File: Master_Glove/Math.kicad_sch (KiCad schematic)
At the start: 0 parts

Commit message: Circuit Log+Sub fait
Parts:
- added D2: 1N4148WS, Diode_SMD:D_SOD-323, symbol Diode:1N4148WS
- added R1: 4.7k, symbol Device:R
- added R2, R3: 2.2k, symbol Device:R
- added R4, R5: 37.4k, symbol Device:R
- added R6, R7: 10k, symbol Device:R
- added U1: OPA2340, symbol Amplifier_Operational:OPA2340
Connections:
- new net: D2.2 (A), R1.2, U1.2 (-)
- new net: R3.1, R5.1, U1.5 (+)
- new net: R3.2, R6.1
- new net: R2.1, R7.1
- new net: R2.2, R4.1, U1.6 (-)
- new net +5V: R6.2, U1.8 (V+)
- new net DiffOutput: R4.2, U1.7
- new net GND: R5.2, U1.3 (+), U1.4 (V-)
- new net LogOutput: D2.1 (K), R7.2, U1.1
- new net SignalInput: R1.1
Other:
- note added: "*3.1076 & Substractor"
- note added: "Log Amplifier, Output = ln(Input)"
- note added: "OP Amp Power"
- note added: "Vout = ln(Vin)"

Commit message: Edit formula with new info
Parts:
- added R11, R12, R13, R14: 10k, symbol Device:R
- added U2: OPA2340, symbol Amplifier_Operational:OPA2340
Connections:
- net +5V: now also R12.2, U2.8 (V+); no longer R6.2
- net GND: now also R7.2, R13.2, U2.4 (V-)
- net LogOutput: now also R6.2; no longer R7.2
- net DiffOutput renamed GainOutput
- net GainOutput: now also R11.1, R14.2, U2.1
- new net: R11.2, R14.1, U2.2 (-)
- new net: R12.1, R13.1, U2.3 (+)
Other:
- note added: "*3.1076"
- note added: "Unused"
- note removed: "*3.1076 & Substractor"

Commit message: work on discharge
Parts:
- added C5, C6: 100nF, symbol Device:C
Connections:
- net +5V: now also C5.1, C6.1
- net GND: now also C5.2, C6.2
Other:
- moved on the sheet: U1C, U2C

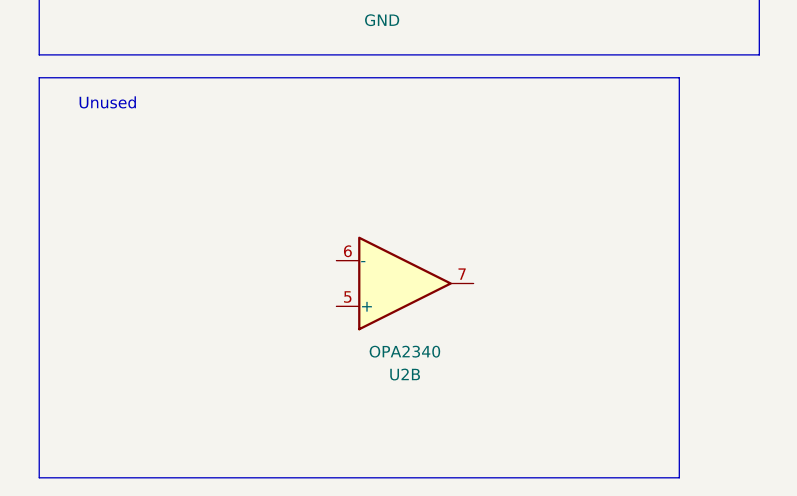
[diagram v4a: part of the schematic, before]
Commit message: Working on emitter Circuit
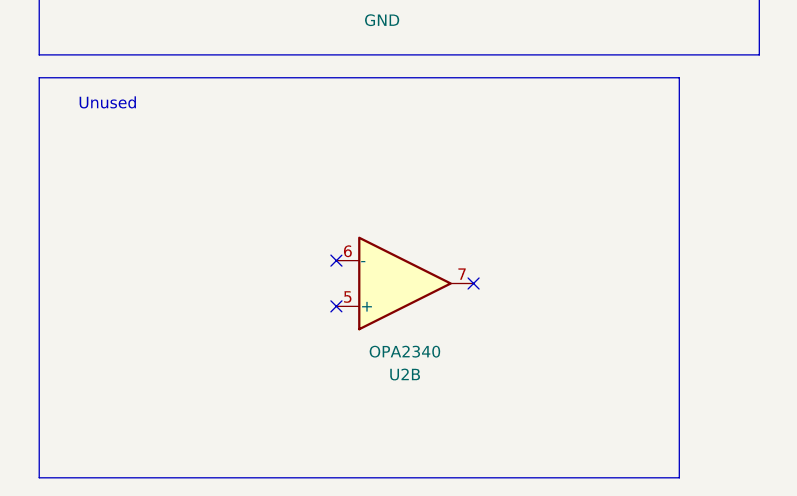
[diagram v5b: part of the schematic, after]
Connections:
- no-connect marks 0 -> 3
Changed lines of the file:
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@@
 		(color 0 0 0 0)
+	)
+	(no_connect
+		(at 156.21 91.44)
+	)
+	(no_connect
+		(at 171.45 93.98)
+	)
+	(no_connect
+		(at 156.21 96.52)
 	)
 	(wire

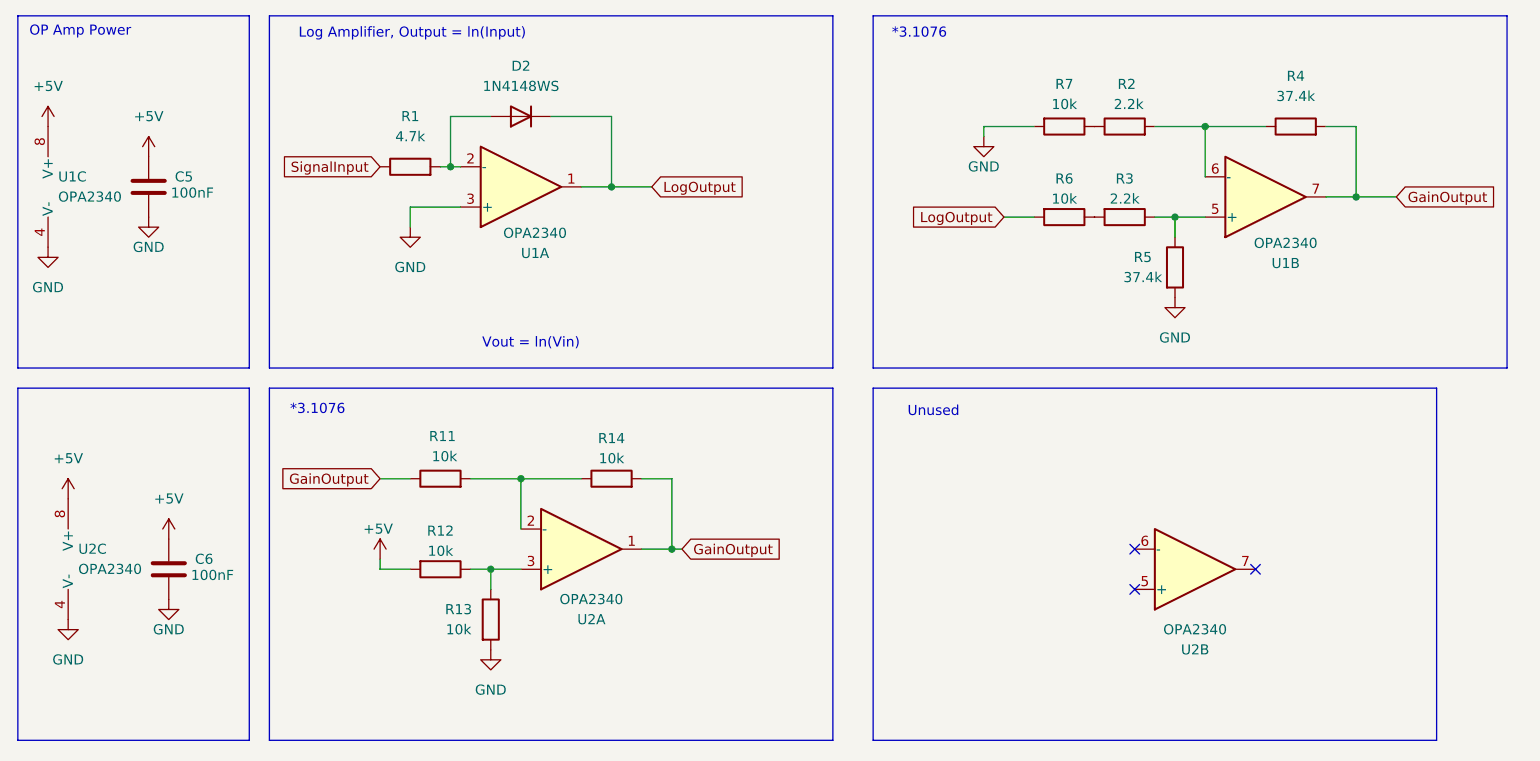
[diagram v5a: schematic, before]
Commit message: Circuit ready for review
Added connection to sensor with push-pull output circuit and changed resistances to be U.S.A. format
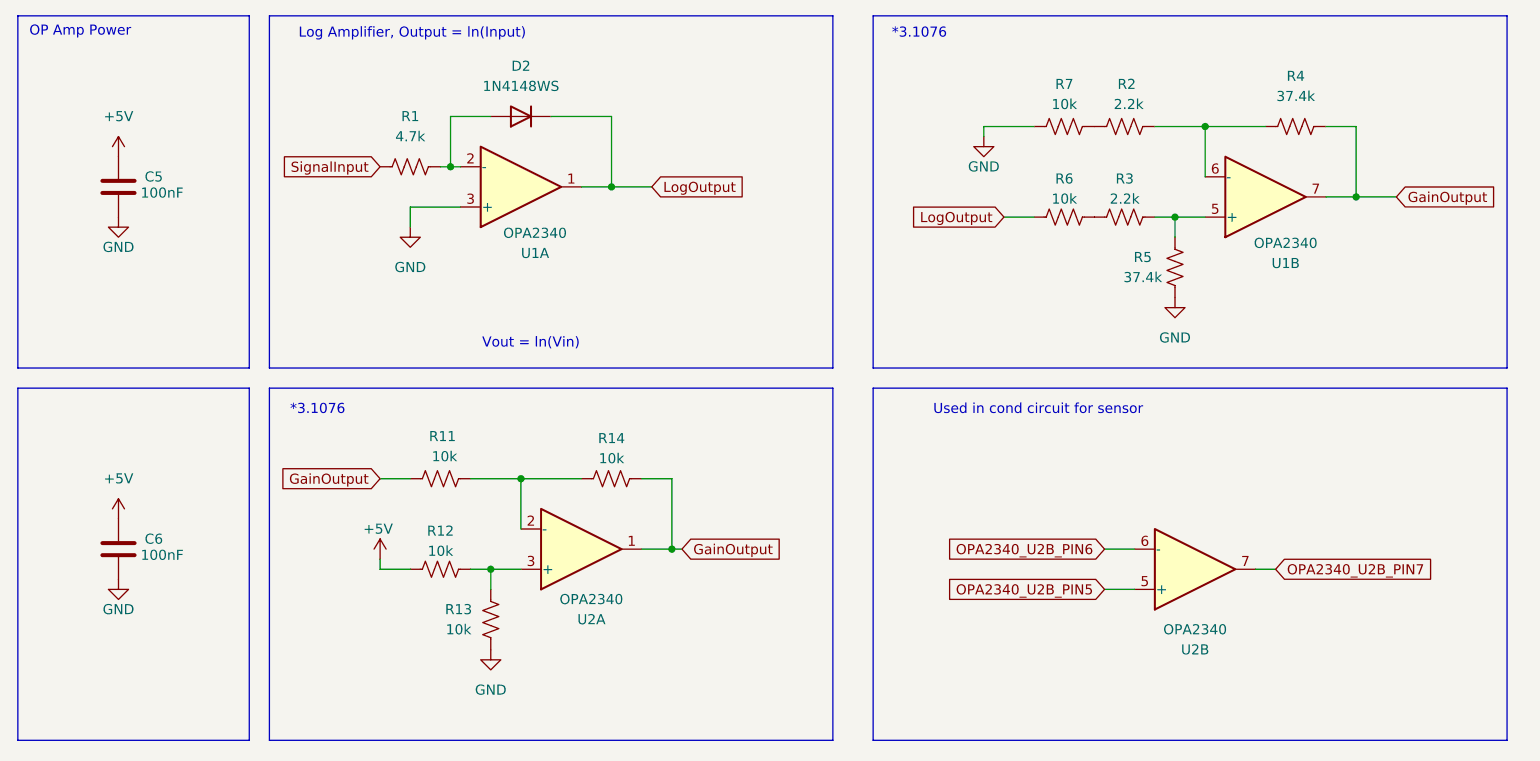
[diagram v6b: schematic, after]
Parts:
- removed unit 3 of U1
- removed unit 3 of U2
- R1, R11, R12, R13, R14, R2, R3, R4, R5, R6, R7: symbol Device:R -> Device:R_US
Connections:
- net OPA2340_U2B_PIN5: now reaches U2.5 (+)
- net OPA2340_U2B_PIN6: now reaches U2.6 (-)
- net OPA2340_U2B_PIN7: now reaches U2.7
- no-connect marks 3 -> 0
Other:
- note added: "Used in cond circuit for sensor"
- note removed: "Unused"
- moved on the sheet: C5, C6

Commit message: Simplifications and modifications following Myriam Recommendation
Circuit will be validated this weekend by Myriam
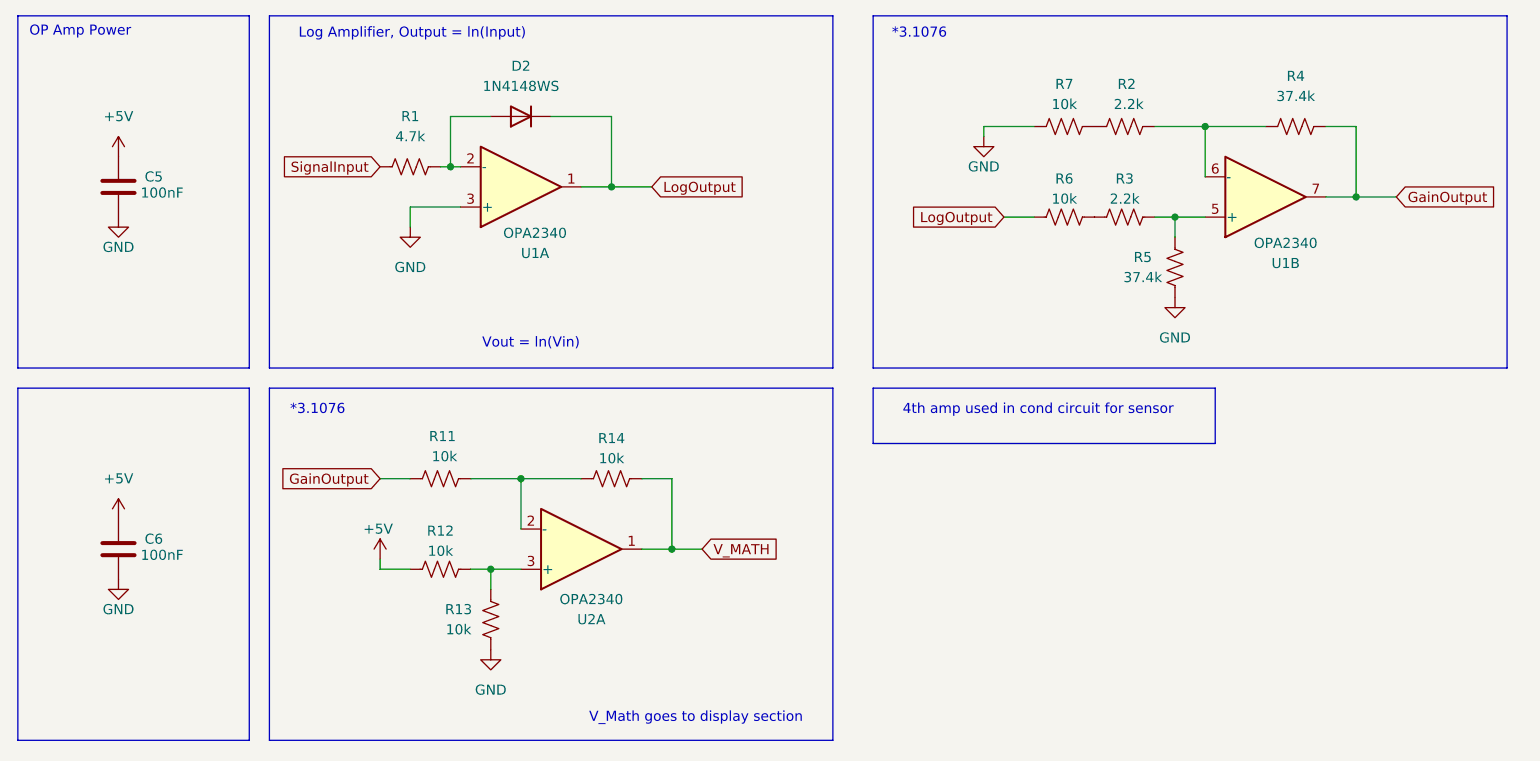
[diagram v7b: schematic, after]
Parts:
- removed unit 2 of U2
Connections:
- net GainOutput: no longer R14.2, U2.1
- new net V_MATH: R14.2, U2.1
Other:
- note added: "4th amp used in cond circuit for sensor"
- note added: "V_Math goes to display section"
- note removed: "Used in cond circuit for sensor"
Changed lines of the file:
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@@
 	(rectangle
 		(start 123.19 71.12)
-		(end 203.2 115.57)
+		(end 166.37 78.105)
 		(stroke
 			(width 0)
@@
 		)
 	)
+	(text "V_Math goes to display section"
+		(exclude_from_sim no)
+		(at 100.838 112.776 0)
+		(effects
+			(font
+				(size 1.27 1.27)
+			)
+		)
+	)
 	(text "*3.1076"
 		(exclude_from_sim no)
@@
 		)
 	)
-	(text "Used in cond circuit for sensor"
+	(text "4th amp used in cond circuit for sensor"
 		(exclude_from_sim no)
 		(at 144.018 73.914 0)
@@
 	(wire
 		(pts
-			(xy 152.4 96.52) (xy 156.21 96.52)
-		)
-		(stroke
-			(width 0)
-			(type default)
-		)
-	)
-	(wire
-		(pts
 			(xy 74.93 93.98) (xy 72.39 93.98)
 		)
@@
 	(wire
 		(pts
+			(xy 97.79 82.55) (xy 97.79 91.44)
+		)
+		(stroke
+			(width 0)
+			(type default)
+		)
+	)
+	(wire
+		(pts
 			(xy 161.29 49.53) (xy 165.1 49.53)
 		)
@@
 	(wire
 		(pts
+			(xy 101.6 91.44) (xy 97.79 91.44)
+		)
+		(stroke
+			(width 0)
+			(type default)
+		)
+	)
+	(wire
+		(pts
 			(xy 165.1 44.45) (xy 165.1 38.1)
 		)
@@
 	(wire
 		(pts
-			(xy 152.4 91.44) (xy 156.21 91.44)
-		)
-		(stroke
-			(width 0)
-			(type default)
-		)
-	)
-	(wire
-		(pts
-			(xy 173.99 93.98) (xy 171.45 93.98)
-		)
-		(stroke
-			(width 0)
-			(type default)
-		)
-	)
-	(wire
-		(pts
 			(xy 161.29 49.53) (xy 158.75 49.53)
 		)
@@
 	(wire
 		(pts
-			(xy 97.79 91.44) (xy 99.06 91.44)
-		)
-		(stroke
-			(width 0)
-			(type default)
-		)
-	)
-	(wire
-		(pts
 			(xy 68.58 43.18) (xy 69.85 43.18)
 		)
@@
 	(wire
 		(pts
-			(xy 97.79 82.55) (xy 97.79 91.44)
-		)
-		(stroke
-			(width 0)
-			(type default)
-		)
-	)
-	(wire
-		(pts
 			(xy 90.17 36.83) (xy 90.17 45.72)
 		)
@@
 			(width 0)
 			(type default)
-		)
-	)
-	(global_label "OPA2340_U2B_PIN7"
-		(shape input)
-		(at 173.99 93.98 0)
-		(fields_autoplaced yes)
-		(effects
-			(font
-				(size 1.27 1.27)
-			)
-			(justify left)
-		)
-		(property "Intersheetrefs" "${INTERSHEET_REFS}"
-			(at 195.6623 93.98 0)
-			(effects
-				(font
-					(size 1.27 1.27)
-				)
-				(justify left)
-				(hide yes)
-			)
 		)
 	)
@@
 		)
 	)
-	(global_label "OPA2340_U2B_PIN6"
+	(global_label "V_MATH"
 		(shape input)
-		(at 152.4 91.44 180)
+		(at 101.6 91.44 0)
 		(fields_autoplaced yes)
 		(effects
@@
 				(size 1.27 1.27)
 			)
-			(justify right)
+			(justify left)
 		)
 		(property "Intersheetrefs" "${INTERSHEET_REFS}"
-			(at 130.7277 91.44 0)
-			(effects
-				(font
-					(size 1.27 1.27)
-				)
-				(justify right)
+			(at 111.4795 91.44 0)
+			(effects
+				(font
+					(size 1.27 1.27)
+				)
+				(justify left)
 				(hide yes)
 			)
@@
 		)
 	)
-	(global_label "OPA2340_U2B_PIN5"
-		(shape input)
-		(at 152.4 96.52 180)
-		(fields_autoplaced yes)
-		(effects
-			(font
-				(size 1.27 1.27)
-			)
-			(justify right)
-		)
-		(property "Intersheetrefs" "${INTERSHEET_REFS}"
-			(at 130.7277 96.52 0)
-			(effects
-				(font
-					(size 1.27 1.27)
-				)
-				(justify right)
-				(hide yes)
-			)
-		)
-	)
 	(global_label "LogOutput"
 		(shape input)
@@
 		)
 	)
-	(global_label "GainOutput"
-		(shape input)
-		(at 99.06 91.44 0)
-		(fields_autoplaced yes)
-		(effects
-			(font
-				(size 1.27 1.27)
-			)
-			(justify left)
-		)
-		(property "Intersheetrefs" "${INTERSHEET_REFS}"
-			(at 112.4469 91.44 0)
-			(effects
-				(font
-					(size 1.27 1.27)
-				)
-				(justify left)
-				(hide yes)
-			)
-		)
-	)
 	(global_label "LogOutput"
 		(shape input)
@@
 					(unit 1)
 				)
-			)
-		)
-	)
-	(symbol
-		(lib_id "Amplifier_Operational:OPA2340")
-		(at 163.83 93.98 0)
-		(mirror x)
-		(unit 2)
-		(exclude_from_sim no)
-		(in_bom yes)
-		(on_board yes)
-		(dnp no)
-		(property "Reference" "U2"
-			(at 163.83 104.14 0)
-			(effects
-				(font
-					(size 1.27 1.27)
-				)
-			)
-		)
-		(property "Value" "OPA2340"
-			(at 163.83 101.6 0)
-			(effects
-				(font
-					(size 1.27 1.27)
-				)
-			)
-		)
-		(property "Footprint" ""
-			(at 163.83 93.98 0)
-			(effects
-				(font
-					(size 1.27 1.27)
-				)
-				(hide yes)
-			)
-		)
-		(property "Datasheet" "http://www.ti.com/lit/ds/symlink/opa4340.pdf"
-			(at 163.83 93.98 0)
-			(effects
-				(font
-					(size 1.27 1.27)
-				)
-				(hide yes)
-			)
-		)
-		(property "Description" "Dual Single-Supply, Rail-to-Rail Operational Amplifiers, MicroAmplifier Series, DIP-8/SOIC-8/SSOP-8"
-			(at 163.83 93.98 0)
-			(effects
-				(font
-					(size 1.27 1.27)
-				)
-				(hide yes)
-			)
-		)
-		(pin "5"
-		)
-		(pin "7"
-		)
-		(pin "3"
-		)
-		(pin "2"
-		)
-		(pin "1"
-		)
-		(pin "6"
-		)
-		(pin "8"
-		)
-		(pin "4"
-		)
-		(instances
-			(project ""
-				(path "/4d29d845-b206-46d3-9e63-0d81f5289579/14bd897f-7c8e-4316-b30e-ec0d722b1f87"
-					(reference "U2")
-					(unit 2)
-				)
-			)
-			(project "Math"
-				(path "/55d98218-baf0-4431-bb29-6996693fa2f6"
-					(reference "U3")
-					(unit 1)
-				)

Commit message: Modifications according to reccomendation
Changed Vcc to +5V
Subbed MIC1551 to MIC 1553
Added debounce on button
Fixed other small bugs
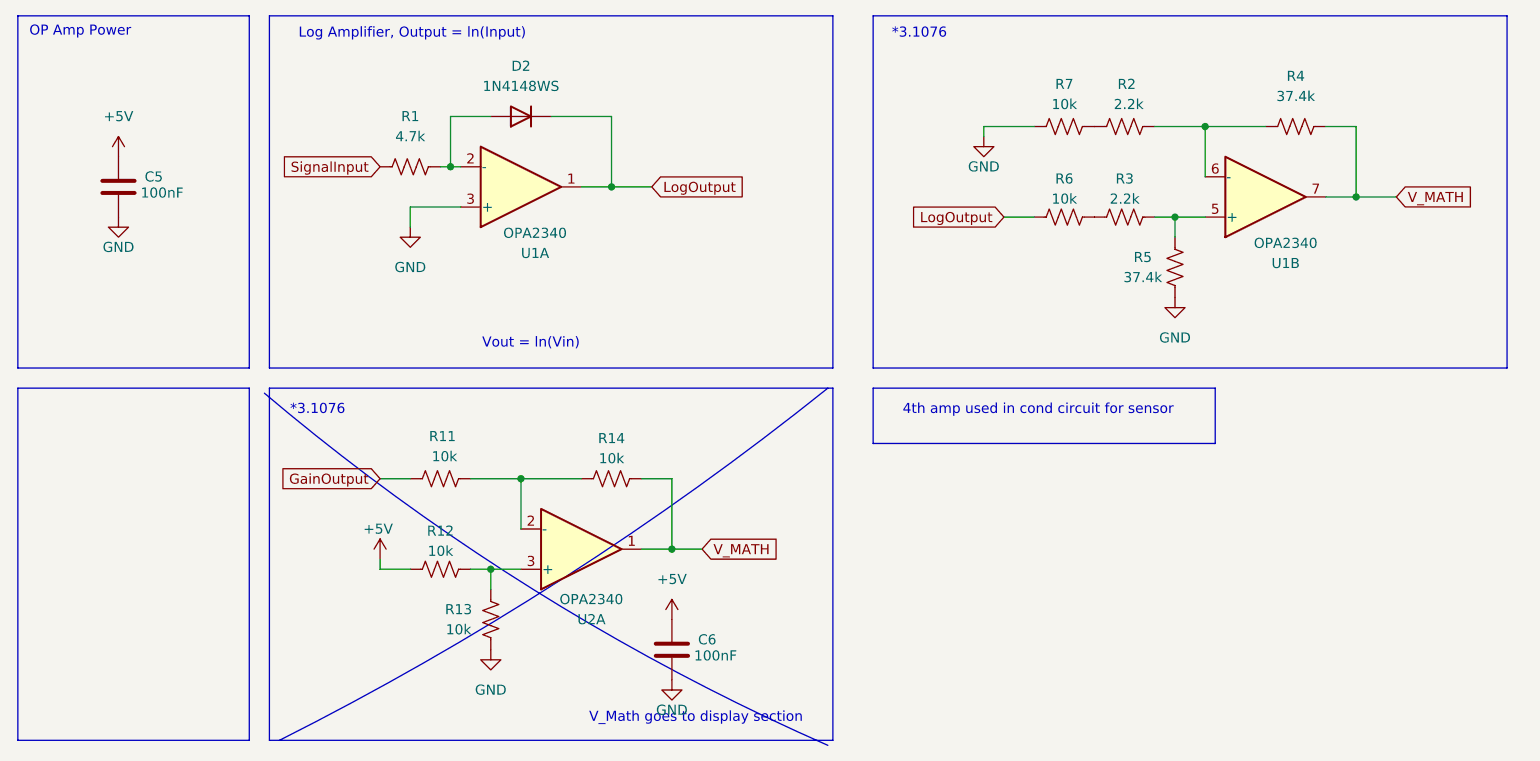
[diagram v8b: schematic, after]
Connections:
- net GainOutput: no longer R4.2, U1.7
- net V_MATH: now also R4.2, U1.7
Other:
- moved on the sheet: C6
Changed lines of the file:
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@@
+		)
+	)
+	(arc
+		(start 117.475 116.205)
+		(mid 80.3141 96.5414)
+		(end 46.355 71.755)
+		(stroke
+			(width 0)
+			(type default)
+		)
+		(fill
+			(type none)
+		)
+	)
+	(arc
+		(start 117.475 71.12)
+		(mid 84.029 95.1536)
+		(end 48.26 115.57)
+		(stroke
+			(width 0)
+			(type default)
+		)
+		(fill
+			(type none)
 		)
 	)
@@
 			(width 0)
 			(type default)
+		)
+	)
+	(global_label "V_MATH"
+		(shape input)
+		(at 189.23 46.99 0)
+		(fields_autoplaced yes)
+		(effects
+			(font
+				(size 1.27 1.27)
+			)
+			(justify left)
+		)
+		(property "Intersheetrefs" "${INTERSHEET_REFS}"
+			(at 199.1095 46.99 0)
+			(effects
+				(font
+					(size 1.27 1.27)
+				)
+				(justify left)
+				(hide yes)
+			)
 		)
 	)
@@
 		)
 	)
-	(global_label "GainOutput"
-		(shape input)
-		(at 189.23 46.99 0)
-		(fields_autoplaced yes)
-		(effects
-			(font
-				(size 1.27 1.27)
-			)
-			(justify left)
-		)
-		(property "Intersheetrefs" "${INTERSHEET_REFS}"
-			(at 202.6169 46.99 0)
-			(effects
-				(font
-					(size 1.27 1.27)
-				)
-				(justify left)
-				(hide yes)
-			)
-		)
-	)
 	(global_label "V_MATH"
 		(shape input)
@@
 	(symbol
 		(lib_id "Device:C")
-		(at 27.94 91.44 0)
+		(at 97.79 104.14 0)
 		(unit 1)
 		(exclude_from_sim no)
@@
 		(dnp no)
 		(property "Reference" "C6"
-			(at 31.242 90.17 0)
+			(at 101.092 102.87 0)
 			(effects
 				(font
@@
 		)
 		(property "Value" "100nF"
-			(at 30.734 92.202 0)
+			(at 100.584 104.902 0)
 			(effects
 				(font
@@
 		)
 		(property "Footprint" ""
-			(at 28.9052 95.25 0)
+			(at 98.7552 107.95 0)
 			(effects
 				(font
@@
 		)
 		(property "Datasheet" "~"
-			(at 27.94 91.44 0)
+			(at 97.79 104.14 0)
 			(effects
 				(font
@@
 		)
 		(property "Description" "Unpolarized capacitor"
-			(at 27.94 91.44 0)
+			(at 97.79 104.14 0)
 			(effects
 				(font
@@
 	(symbol
 		(lib_id "power:+5V")
-		(at 27.94 87.63 0)
+		(at 97.79 100.33 0)
 		(unit 1)
 		(exclude_from_sim no)
@@
 		(fields_autoplaced yes)
 		(property "Reference" "#PWR022"
-			(at 27.94 91.44 0)
+			(at 97.79 104.14 0)
 			(effects
 				(font
@@
 		)
 		(property "Value" "+5V"
-			(at 27.94 82.55 0)
+			(at 97.79 95.25 0)
 			(effects
 				(font
@@
 		)
 		(property "Footprint" ""
-			(at 27.94 87.63 0)
+			(at 97.79 100.33 0)
 			(effects
 				(font
@@
 		)
 		(property "Datasheet" ""
-			(at 27.94 87.63 0)
+			(at 97.79 100.33 0)
 			(effects
 				(font
@@
 		)
 		(property "Description" "Power symbol creates a global label with name \"+5V\""
-			(at 27.94 87.63 0)
+			(at 97.79 100.33 0)
 			(effects
 				(font
@@
 	(symbol
 		(lib_id "power:GND")
-		(at 27.94 95.25 0)
+		(at 97.79 107.95 0)
 		(unit 1)
 		(exclude_from_sim no)
@@
 		(dnp no)
 		(property "Reference" "#PWR023"
-			(at 27.94 101.6 0)
+			(at 97.79 114.3 0)
 			(effects
 				(font
@@
 		)
 		(property "Value" "GND"
-			(at 27.94 99.06 0)
+			(at 97.79 111.76 0)
 			(effects
 				(font
@@
 		)
 		(property "Footprint" ""
-			(at 27.94 95.25 0)
+			(at 97.79 107.95 0)
 			(effects
 				(font
@@
 		)
 		(property "Datasheet" ""
-			(at 27.94 95.25 0)
+			(at 97.79 107.95 0)
 			(effects
 				(font
@@
 		)
 		(property "Description" "Power symbol creates a global label with name \"GND\" , ground"
-			(at 27.94 95.25 0)
-			(effects
-				(font
+			(at 97.79 107.95 0)
+			(effects
+				(font
